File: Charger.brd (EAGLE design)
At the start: 26.4 x 22.4 mm, 15 parts, among them Q1 SPP80P06P

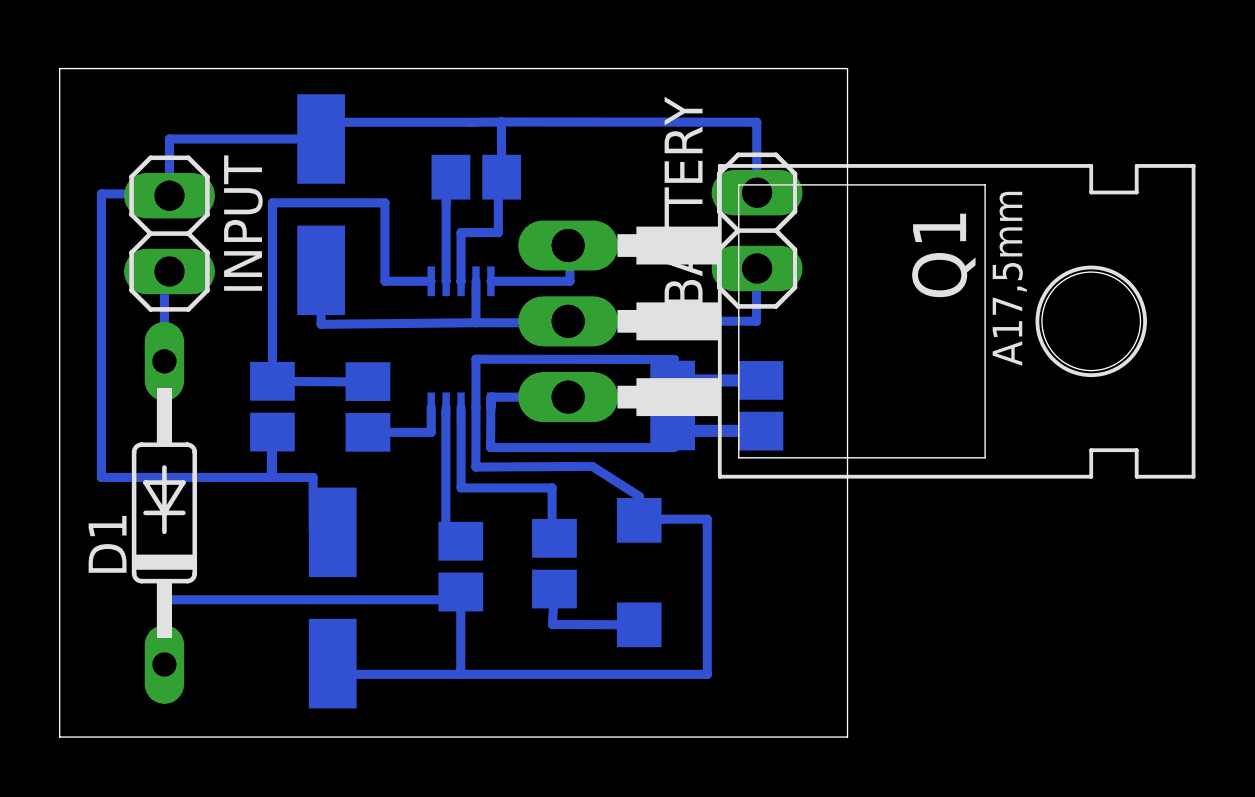
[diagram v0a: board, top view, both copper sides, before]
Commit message: Revert "Add values of capacitors and parallel resistors"
This reverts commit c5449c38890c53df2ecf398a39eaa116fb527d7b.
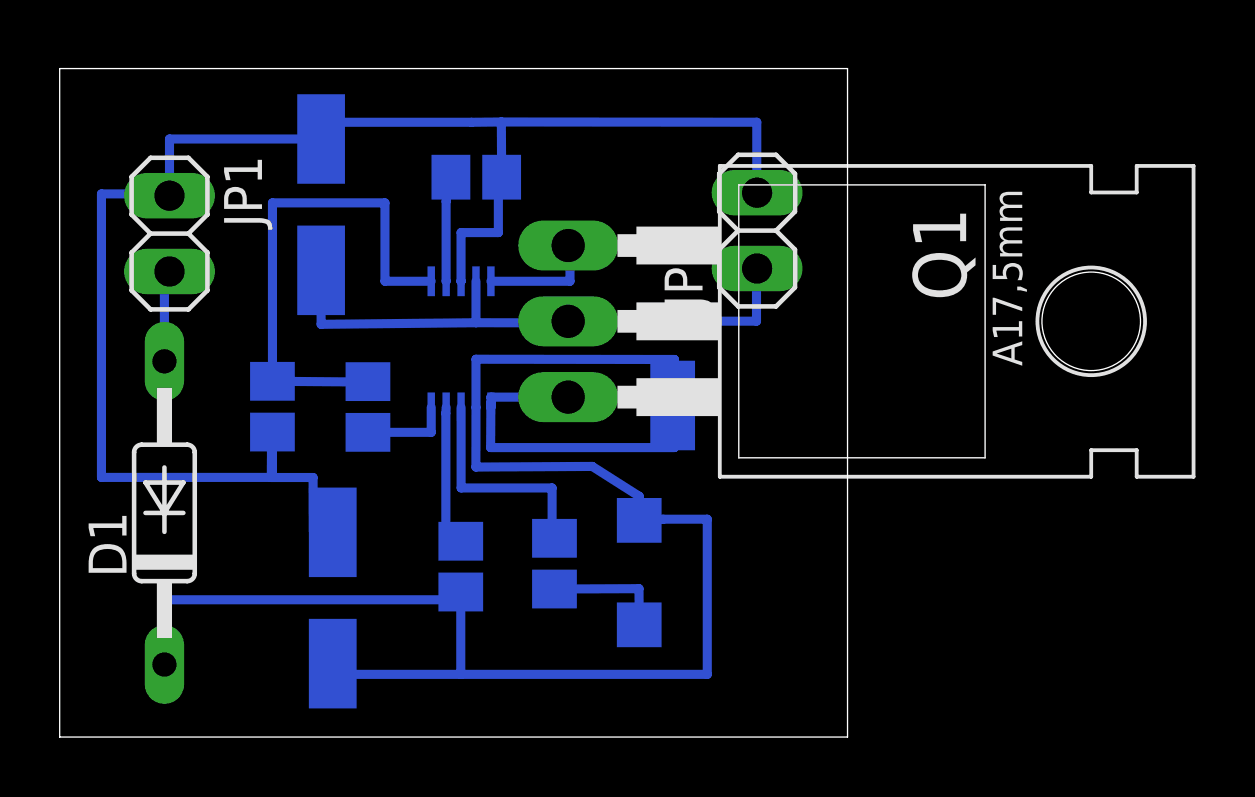
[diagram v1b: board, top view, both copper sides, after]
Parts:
- removed R6: 0.5, resistor:R0805
- C1, C3: value 4.7u -> (none)
- C2: value 0.22u -> (none)
- R1: value 0.5 -> 0.22
- renumbered BATTERY to JP2, INPUT to JP1
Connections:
- net N$1: no longer R6.1
- net N$2: no longer R6.2
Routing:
- net N$1: track 56.2 -> 53.2 mm
- net N$2: track 14.3 -> 11.4 mm
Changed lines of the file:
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@@
 <element name="U$1" library="mcp73841" package="MSOP10" value="MCP73841" x="13.45" y="13.16" rot="MR0"/>
 <element name="D1" library="diode" package="DO35-10" value="1N4148DO35-10" x="3.51" y="7.51" rot="R90"/>
-<element name="R1" library="resistor" package="R0805" value="0.5" x="20.54" y="11.11" rot="MR270"/>
+<element name="R1" library="resistor" package="R0805" value="0.22" x="20.54" y="11.11" rot="MR270"/>
 <element name="R2" library="resistor" package="R0805" value="100k" x="13.44" y="5.71" rot="MR90"/>
 <element name="LED1" library="led" package="CHIPLED_1206" value="" x="19.42" y="5.51" rot="MR180"/>
 <element name="Q1" library="transistor-fet" package="TO220" value="SPP80P06P" x="23.39" y="13.93" rot="R270"/>
-<element name="C1" library="resistor" package="153CLV-0505" value="4.7u" x="8.76" y="17.84" rot="MR270"/>
-<element name="C2" library="resistor" package="C0805" value="0.22u" x="13.96" y="18.76" rot="MR180"/>
-<element name="C3" library="resistor" package="153CLV-0505" value="4.7u" x="9.15" y="4.66" rot="MR270"/>
+<element name="C1" library="resistor" package="153CLV-0505" value="" x="8.76" y="17.84" rot="MR270"/>
+<element name="C2" library="resistor" package="C0805" value="" x="13.96" y="18.76" rot="MR180"/>
+<element name="C3" library="resistor" package="153CLV-0505" value="" x="9.15" y="4.66" rot="MR270"/>
 <element name="R3" library="resistor" package="R0805" value="18k" x="10.33" y="11.06" rot="MR270"/>
 <element name="R4" library="resistor" package="R0805" value="10k" x="7.13" y="11.07" rot="MR90"/>
 <element name="R5" library="resistor" package="R0805" value="510" x="16.58" y="5.81" rot="MR90"/>
-<element name="INPUT" library="pinhead" package="1X02" value="" x="3.68" y="16.87" rot="R270"/>
-<element name="BATTERY" library="pinhead" package="1X02" value="" x="23.37" y="16.97" rot="R90"/>
-<element name="R6" library="resistor" package="R0805" value="0.5" x="23.5" y="11.1" rot="MR270"/>
+<element name="JP1" library="pinhead" package="1X02" value="" x="3.68" y="16.87" rot="R270"/>
+<element name="JP2" library="pinhead" package="1X02" value="" x="23.37" y="16.97" rot="R90"/>
 </elements>
 <signals>
@@
 <wire x1="9.15" y1="2.46" x2="9.15" y2="2.1" width="0.3048" layer="16"/>
 <wire x1="9.15" y1="2.1" x2="13.44" y2="2.1" width="0.3048" layer="16"/>
-<contactref element="R6" pad="1"/>
-<wire x1="23.5" y1="11.95" x2="20.54" y2="11.95" width="0.4064" layer="16"/>
-<wire x1="20.54" y1="11.95" x2="20.54" y2="11.96" width="0.4064" layer="16"/>
 </signal>
 <signal name="N$2">
@@
 <wire x1="17.04" y1="11.39" x2="14.45" y2="11.39" width="0.3048" layer="16"/>
 <wire x1="14.45" y1="11.39" x2="14.45" y2="11.0469" width="0.3048" layer="16"/>
-<contactref element="R6" pad="2"/>
-<wire x1="20.6" y1="10.26" x2="23.5" y2="10.26" width="0.4064" layer="16"/>
-<wire x1="23.5" y1="10.26" x2="23.5" y2="10.25" width="0.4064" layer="16"/>
 </signal>
 <signal name="N$3">
@@
 <contactref element="U$1" pad="9"/>
 <contactref element="C1" pad="+"/>
-<contactref element="BATTERY" pad="1"/>
+<contactref element="JP2" pad="1"/>
 <wire x1="23.35" y1="15.7" x2="23.37" y2="15.7" width="0.3048" layer="16"/>
 <wire x1="13.95" y1="15.2731" x2="13.95" y2="13.88315625" width="0.3048" layer="16"/>
@@
 <contactref element="C3" pad="-"/>
 <contactref element="R4" pad="1"/>
-<contactref element="BATTERY" pad="2"/>
-<contactref element="INPUT" pad="1"/>
+<contactref element="JP2" pad="2"/>
+<contactref element="JP1" pad="1"/>
 <wire x1="23.359665625" y1="18.24" x2="23.37" y2="18.24" width="0.3048" layer="16"/>
 <wire x1="14.8" y1="20.61" x2="23.359665625" y2="20.602309375" width="0.3048" layer="16"/>
@@
 <contactref element="LED1" pad="C"/>
 <contactref element="R5" pad="1"/>
-<wire x1="19.42" y1="3.76" x2="16.5124875" y2="3.771996875" width="0.3048" layer="16"/>
-<wire x1="16.5124875" y1="3.771996875" x2="16.58" y2="4.96" width="0.3048" layer="16"/>
+<wire x1="19.42" y1="3.76" x2="19.4124875" y2="4.971996875" width="0.3048" layer="16"/>
+<wire x1="19.4124875" y1="4.971996875" x2="16.58" y2="4.96" width="0.3048" layer="16"/>
 </signal>
 <signal name="N$6">
@@
 </signal>
 <signal name="N$10">
-<contactref element="INPUT" pad="2"/>
+<contactref element="JP1" pad="2"/>
 <contactref element="D1" pad="A"/>
 <wire x1="3.68" y1="15.6" x2="3.51" y2="15.6" width="0.3048" layer="16"/>
